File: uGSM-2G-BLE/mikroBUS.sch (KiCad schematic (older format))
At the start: 1 part

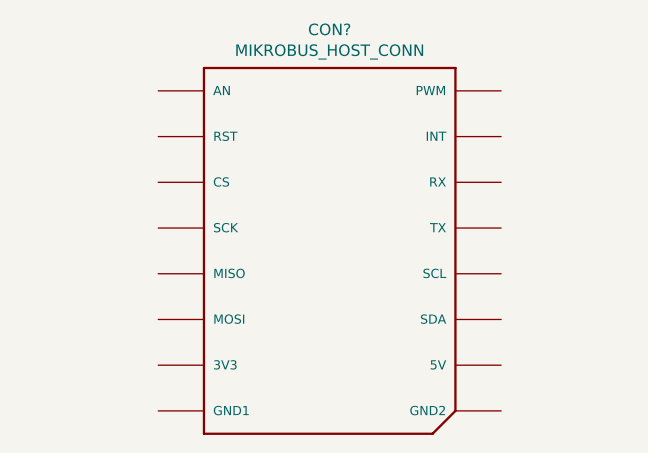
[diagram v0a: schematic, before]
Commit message: ble connected to mikrobus
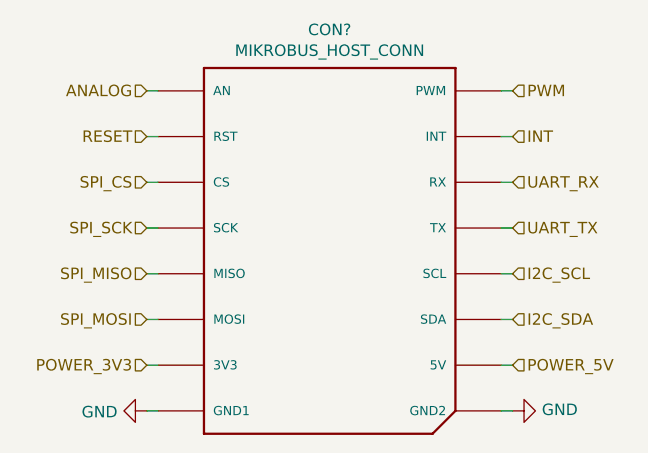
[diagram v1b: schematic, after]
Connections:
- net ANALOG: now reaches CON?.P1 (AN)
- net POWER_5V: now reaches CON?.P10 (5V)
- net I2C_SDA: now reaches CON?.P11 (SDA)
- net I2C_SCL: now reaches CON?.P12 (SCL)
- net UART_TX: now reaches CON?.P13 (TX)
- net UART_RX: now reaches CON?.P14 (RX)
- net INT: now reaches CON?.P15 (INT)
- net PWM: now reaches CON?.P16 (PWM)
- net RESET: now reaches CON?.P2 (RST)
- net SPI_CS: now reaches CON?.P3 (CS)
- net SPI_SCK: now reaches CON?.P4 (SCK)
- net SPI_MISO: now reaches CON?.P5 (MISO)
- net SPI_MOSI: now reaches CON?.P6 (MOSI)
- net POWER_3V3: now reaches CON?.P7 (3V3)
- net GND: now reaches CON?.P8 (GND1)
- net GND: now also CON?.P9 (GND2)
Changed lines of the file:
@@
 	1    0    0    -1
 $EndComp
+Text HLabel 5150 3400 0    50   Input ~ 0
+ANALOG
+Text HLabel 5150 3600 0    50   Input ~ 0
+RESET
+Text HLabel 5150 3800 0    50   Input ~ 0
+SPI_CS
+Text HLabel 5150 4000 0    50   Input ~ 0
+SPI_SCK
+Text HLabel 5150 4200 0    50   Input ~ 0
+SPI_MISO
+Text HLabel 5150 4400 0    50   Input ~ 0
+SPI_MOSI
+Text HLabel 5150 4600 0    50   Input ~ 0
+POWER_3V3
+$Comp
+L power:GND #PWR?
+U 1 1 5E4B0617
+P 5150 4800
+F 0 "#PWR?" H 5150 4550 50  0001 C CNN
+F 1 "GND" V 5155 4672 50  0000 R CNN
+F 2 "" H 5150 4800 50  0001 C CNN
+F 3 "" H 5150 4800 50  0001 C CNN
+	1    5150 4800
+	0    1    1    0
+$EndComp
+$Comp
+L power:GND #PWR?
+U 1 1 5E4B0714
+P 6750 4800
+F 0 "#PWR?" H 6750 4550 50  0001 C CNN
+F 1 "GND" V 6755 4672 50  0000 R CNN
+F 2 "" H 6750 4800 50  0001 C CNN
+F 3 "" H 6750 4800 50  0001 C CNN
+	1    6750 4800
+	0    -1   -1   0
+$EndComp
+Text HLabel 6750 4600 2    50   Input ~ 0
+POWER_5V
+Text HLabel 6750 4400 2    50   Input ~ 0
+I2C_SDA
+Text HLabel 6750 4200 2    50   Input ~ 0
+I2C_SCL
+Text HLabel 6750 4000 2    50   Input ~ 0
+UART_TX
+Text HLabel 6750 3800 2    50   Input ~ 0
+UART_RX
+Text HLabel 6750 3600 2    50   Input ~ 0
+INT
+Text HLabel 6750 3400 2    50   Input ~ 0
+PWM
+Wire Wire Line
+	5200 3400 5150 3400
+Wire Wire Line
+	5150 3600 5200 3600
+Wire Wire Line
+	5150 3800 5200 3800
+Wire Wire Line
+	5150 4000 5200 4000
+Wire Wire Line
+	5150 4200 5200 4200
+Wire Wire Line
+	5150 4400 5200 4400
+Wire Wire Line
+	5150 4600 5200 4600
+Wire Wire Line
+	5200 4800 5150 4800
+Wire Wire Line
+	6700 4800 6750 4800
+Wire Wire Line
+	6700 4600 6750 4600
+Wire Wire Line
+	6750 4400 6700 4400
+Wire Wire Line
+	6700 4200 6750 4200
+Wire Wire Line
+	6750 4000 6700 4000
+Wire Wire Line
+	6750 3800 6700 3800
+Wire Wire Line
+	6700 3600 6750 3600
+Wire Wire Line
+	6700 3400 6750 3400
 $EndSCHEMATC
